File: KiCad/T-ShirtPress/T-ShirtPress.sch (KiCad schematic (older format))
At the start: 49 parts, among them J1 ST_LINKV2, J2 Display, J3 Thermistor, J4 SSR_CONTROL, J5 AC_LINE, J6 AC_NEUTRAL, U1 AMS1117-3.3, U2 STM32F429ZGTx, Y1 8MHz

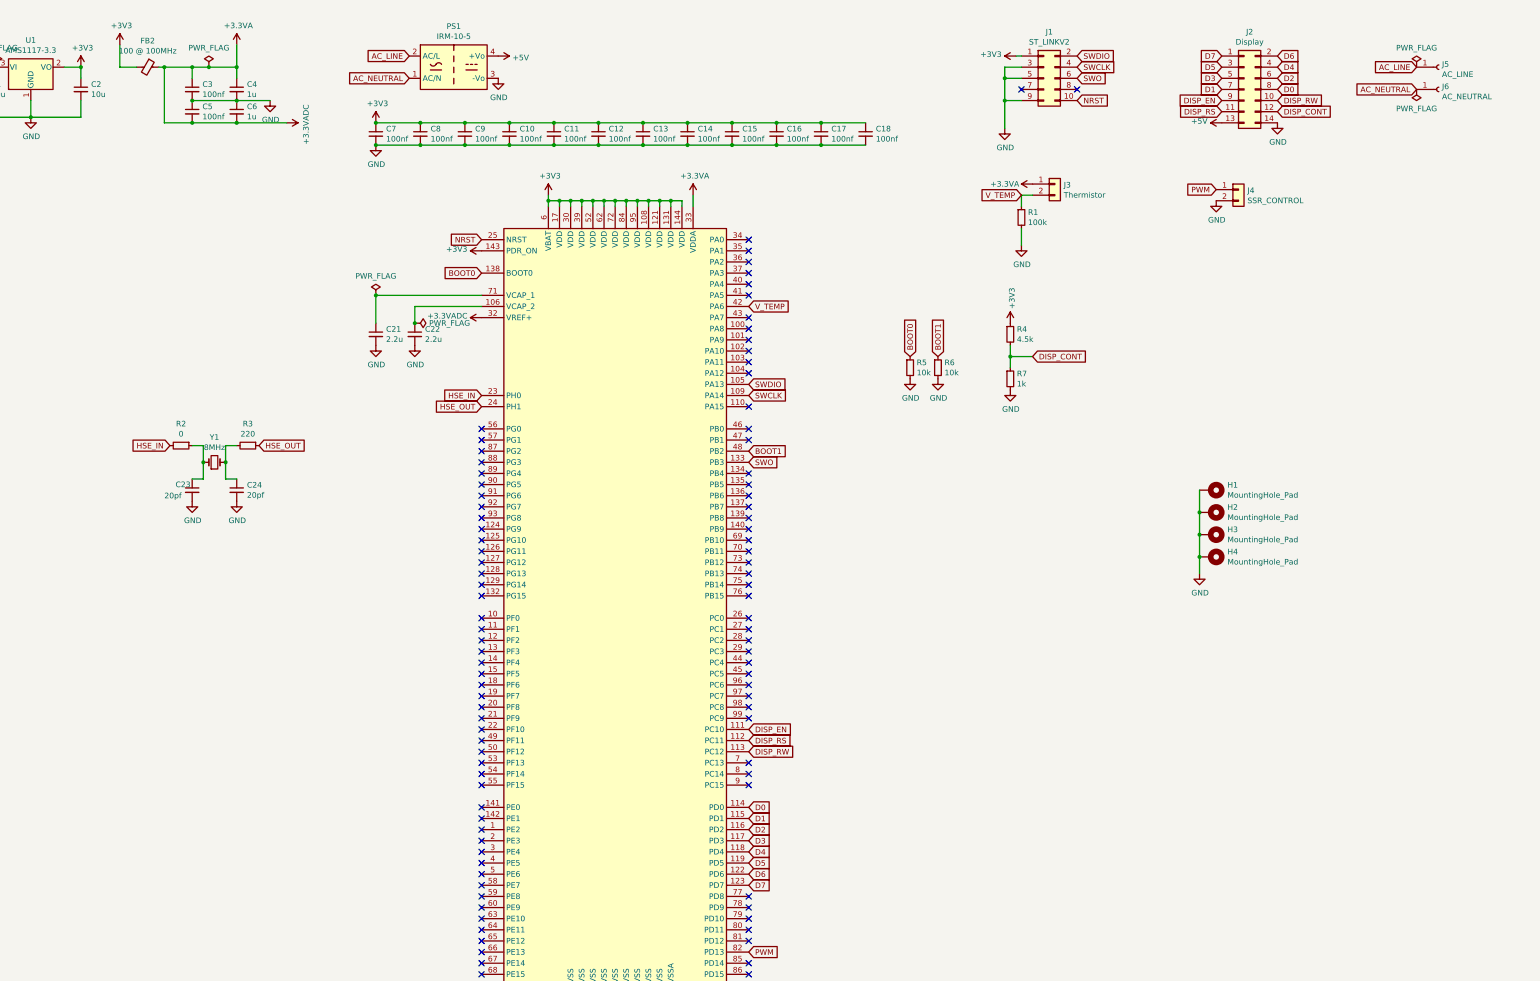
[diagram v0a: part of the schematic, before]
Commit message: PCB Done!
The pcb should be done now and it is ordered with assembly so hopefully everything goes well and it will arrive in roughly a week.
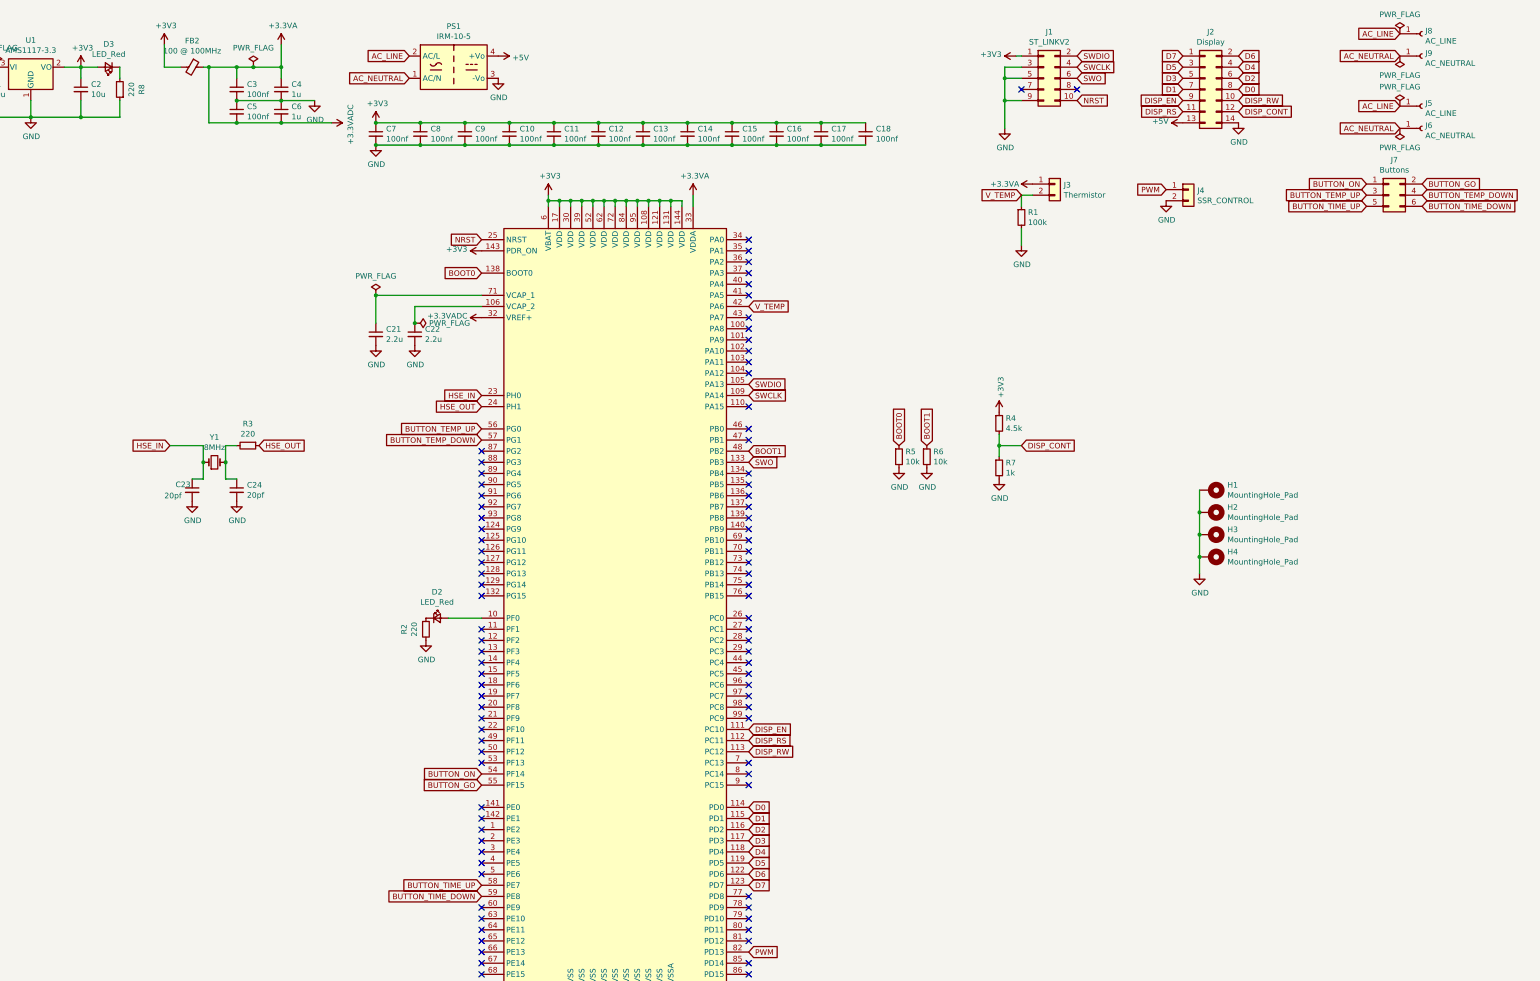
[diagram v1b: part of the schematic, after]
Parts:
- added D2, D3: LED_Red, LED_SMD:LED_0603_1608Metric, symbol Device:LED_Small
- added J7: Buttons, Connector_PinHeader_2.54mm:PinHeader_2x03_P2.54mm_Vertical, symbol Connector_Generic:Conn_02x03_Odd_Even
- added J8: AC_LINE, Connector_Wire:SolderWire-2.5sqmm_1x01_D2.4mm_OD3.6mm, symbol Connector:Conn_01x01_Female
- added J9: AC_NEUTRAL, Connector_Wire:SolderWire-2.5sqmm_1x01_D2.4mm_OD3.6mm, symbol Connector:Conn_01x01_Female
- added R8: 220, Resistor_SMD:R_0603_1608Metric, symbol Device:R_Small
- R2: value 0 -> 220
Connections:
- net +3V3: now also D3.2 (A)
- net AC_LINE: now also J8.1 (Pin_1)
- net AC_NEUTRAL: now also J9.1 (Pin_1)
- net GND: now also R2.2, R8.1
- net HSE_IN: now also C23.1, Y1.1; no longer R2.2
- net at U2.10 (PF0): now also D2.2 (A)
- net BUTTON_ON: now reaches U2.54 (PF14)
- net BUTTON_ON: now also J7.1 (Pin_1)
- net BUTTON_GO: now reaches U2.55 (PF15)
- net BUTTON_GO: now also J7.2 (Pin_2)
- net BUTTON_TEMP_UP: now reaches U2.56 (PG0)
- net BUTTON_TEMP_UP: now also J7.3 (Pin_3)
- net BUTTON_TEMP_DOWN: now reaches U2.57 (PG1)
- net BUTTON_TEMP_DOWN: now also J7.4 (Pin_4)
- net BUTTON_TIME_UP: now reaches U2.58 (PE7)
- net BUTTON_TIME_UP: now also J7.5 (Pin_5)
- net BUTTON_TIME_DOWN: now reaches U2.59 (PE8)
- net BUTTON_TIME_DOWN: now also J7.6 (Pin_6)
- new net: D2.1 (K), R2.1
- new net: D3.1 (K), R8.2
- no-connect marks 97 -> 90
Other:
- moved on the sheet: C3, C4, C5, C6, FB2, J2, J4, J5, J6, R4, R5, R6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
